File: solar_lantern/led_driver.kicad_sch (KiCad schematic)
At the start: 9 parts, among them Q3 RU20P7C, U3 MCP1664

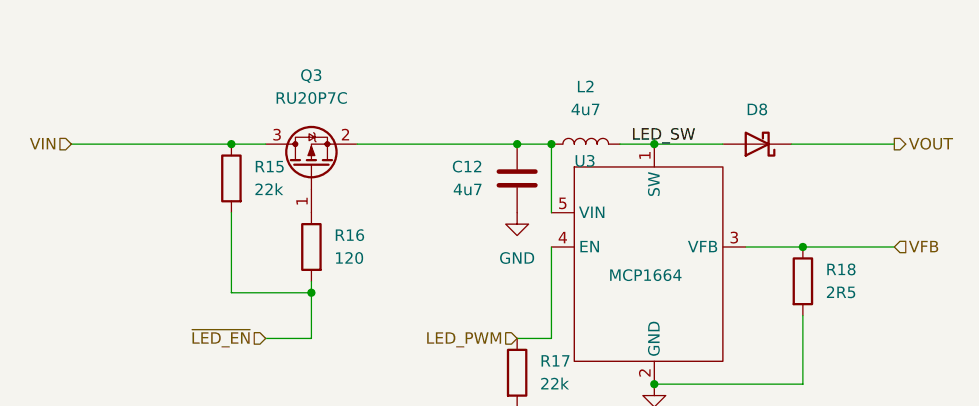
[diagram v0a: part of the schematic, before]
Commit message: Make board smaller, Fix bad cap orientation, Add a diode to reduce quescient current
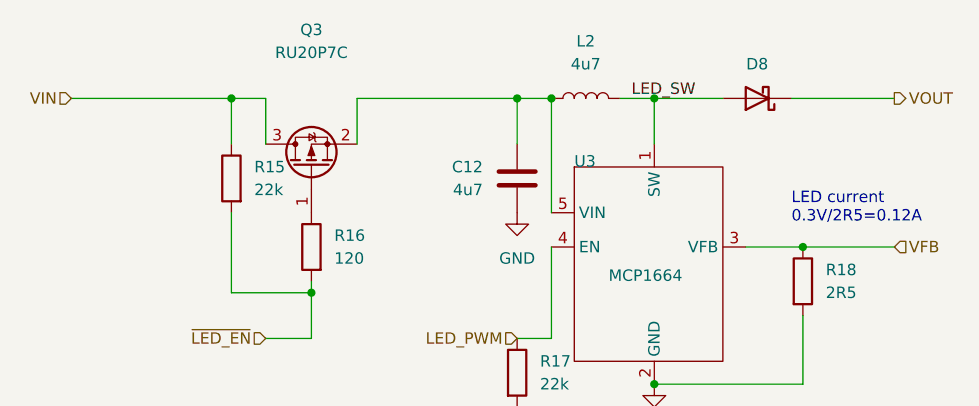
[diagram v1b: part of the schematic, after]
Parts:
- L2: footprint Inductor_SMD:L_Coilcraft_XAL60xx_6.36x6.56mm -> Inductor_SMD:L_Taiyo-Yuden_MD-4040; Manufacturer (none) -> TDK; PartNo (none) -> VLCF4020T-4R7N1R2
- R18: footprint Resistor_SMD:R_0603_1608Metric_Pad0.98x0.95mm_HandSolder -> Resistor_SMD:R_0805_2012Metric; Manufacturer (none) -> Vishay; PartNo (none) -> CRCW08052R49FKEA
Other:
- note added: "LED current 0.3V/2R5=0.12A"
- moved on the sheet: D8, L2

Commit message: Nicen schematics a bit
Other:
- company: (none) -> Catnip electronics
- title: (none) -> LED driver
- moved on the sheet: C12, D8, L2, Q3, R15, R16, R17, R18, U3

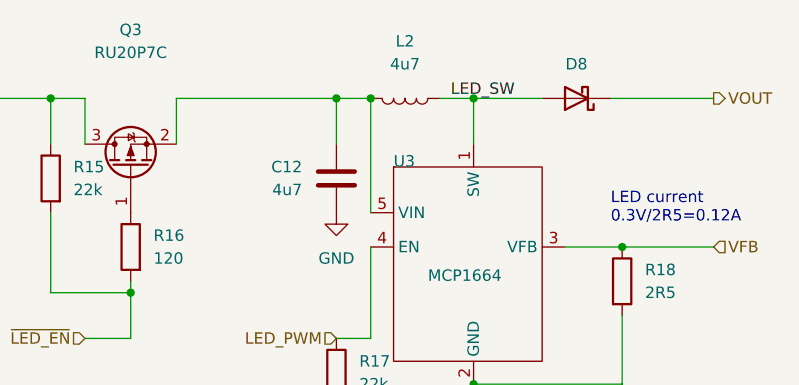
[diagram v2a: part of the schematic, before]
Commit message: Add CERN-OHL_S licence
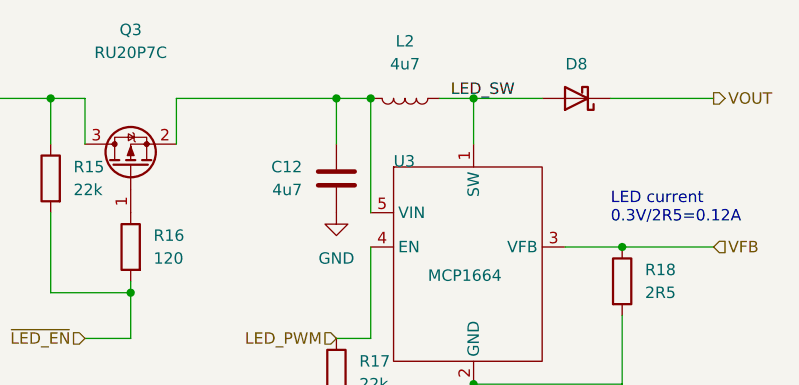
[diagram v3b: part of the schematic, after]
